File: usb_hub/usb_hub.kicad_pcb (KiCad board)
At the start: 2 copper layers, 104 x 50 mm, 143 parts, among them Q1 2N3904, U1 TPS2044B, U10 USB_A_FEMALE, U11 USB_A_FEMALE, U12 SN75240, U13 SN75240, U14 M93C46, U15 USB_A_FEMALE, U16 USB_A_FEMALE, U17 USB_A_FEMALE, U18 USB_A_FEMALE, U2 TPS2044B, U3 TUSB2077A, U4 TPS76333, U5 USB_A_MALE, U6 SN75240, U7 SN75240, U8 SN75240, U9 USB_A_FEMALE, X1 6 MHz

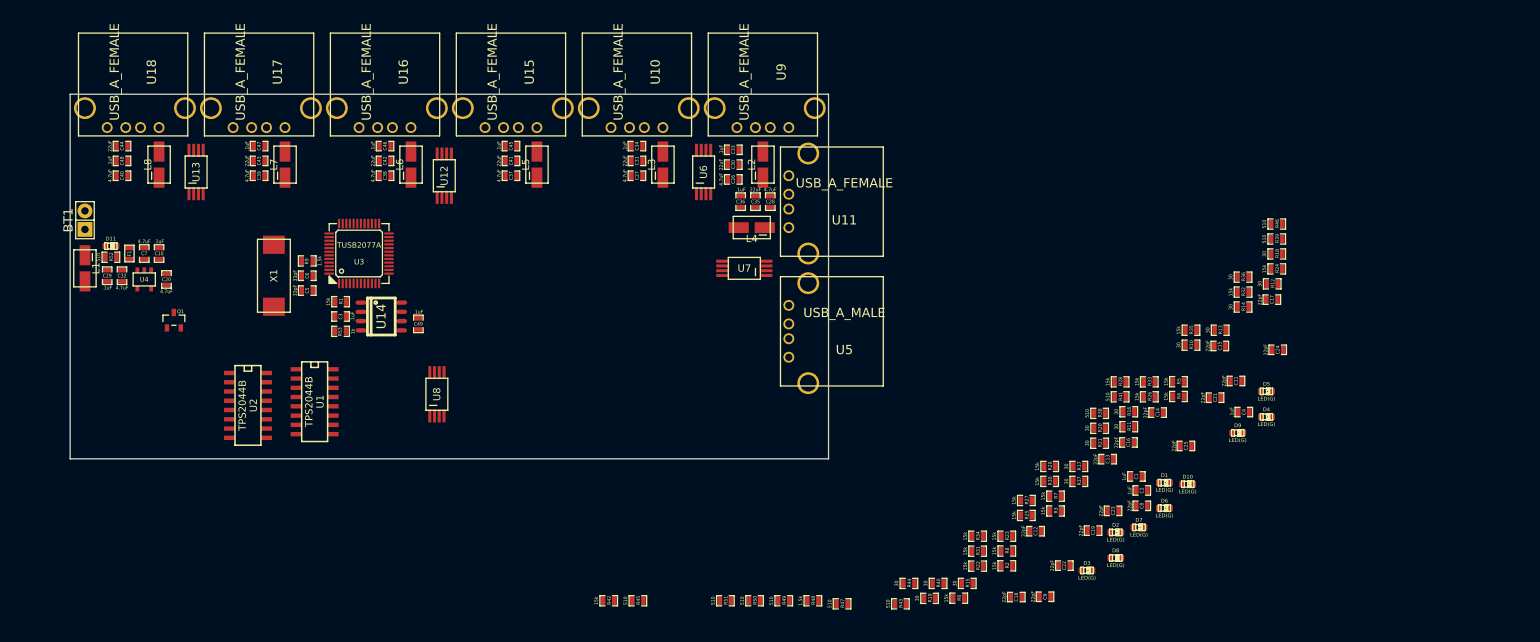
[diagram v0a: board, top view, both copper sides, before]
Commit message: need to not waste as much space on board
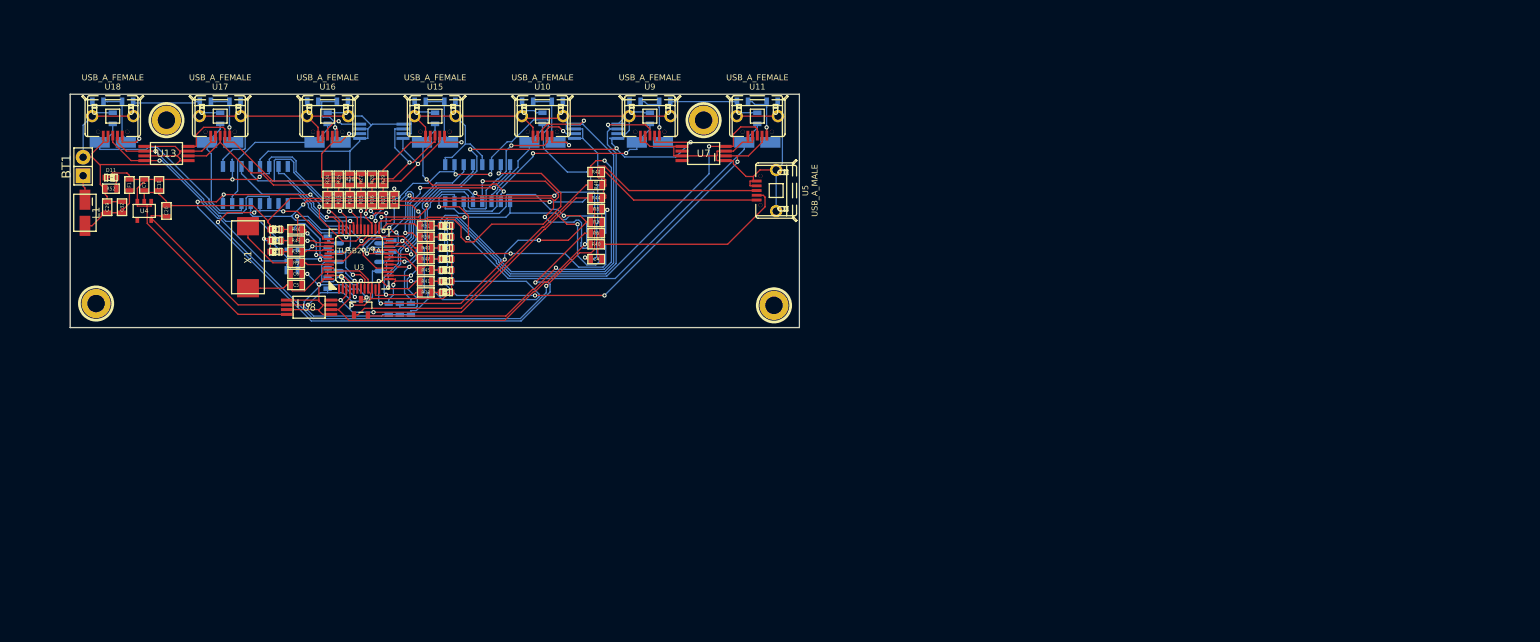
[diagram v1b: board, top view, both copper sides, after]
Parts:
- added 1PIN: P***, Connect:1pin, F.Cu at (48.8, 32.8)
- added 2PIN: P***, Connect:1pin, F.Cu at (122.4, 32.8)
- added 3PIN: P***, Connect:1pin, F.Cu at (132.1, 58.2)
- added 4PIN: P***, Connect:1pin, F.Cu at (39.1, 57.9)
- C1, C11, C12, C13, C14, C15, C16, C18, C19, C2, C21, C22, C23, C24, C25, C26, C27, C28, C3, C30, C31, C33, C34, C35, C36, C37, C38, C39, C40, C41, C42, C43, C44, C45, C46, C47, C48, C49, C8, C9: footprint SMD_Packages:SMD-0603_c -> SMD_Packages:SMD-0603; moved to B.Cu
- C10, C17, C20, C29, C32, C4, C5, C6, C7: footprint SMD_Packages:SMD-0603_c -> SMD_Packages:SMD-0603
- L2, L3, L4, L5, L6, L7, L8, U1, U12, U14, U2, U6: moved to B.Cu
- R1, R10, R11, R18, R19, R20, R21, R22, R23, R3, R30, R31, R32, R33, R34, R35, R36, R37, R4, R5, R53, R7: footprint SMD_Packages:SMD-0603_r -> SMD_Packages:SMD-0603; moved to B.Cu
- R12, R13, R14, R15, R16, R17, R2, R24, R25, R26, R27, R28, R29, R38, R39, R40, R41, R42, R43, R44, R45, R46, R47, R48, R49, R50, R51, R52, R6, R8, R9: footprint SMD_Packages:SMD-0603_r -> SMD_Packages:SMD-0603
- U10, U11, U15, U16, U17, U18, U5, U9: footprint Connect:USB_A -> ab2_usb:AB2_USB_MICRO_SMD
- moved D4 138.0 mm to (63.8, 49.3), turned to 180 degrees
- moved R39 134.5 mm to (66.5, 50.8), turned to 180 degrees
- moved R46 134.5 mm to (66.5, 47.8), turned to 180 degrees
- moved R24 130.7 mm to (70.9, 40.9), turned to 270 degrees
- moved R12 130.0 mm to (70.9, 43.7), turned to 90 degrees
- moved D6 127.7 mm to (63.8, 47.8), turned to 180 degrees
- moved C11 127.0 mm to (70.9, 43.7), turned to 90 degrees
- moved R10 124.3 mm to (65.5, 51.3), turned to 270 degrees
- moved R14 123.4 mm to (73.9, 43.7), turned to 90 degrees
- moved R13 122.2 mm to (72.4, 43.7), turned to 90 degrees
- moved D2 121.5 mm to (63.8, 50.8), turned to 180 degrees
- moved C17 121.1 mm to (80.0, 43.7), turned to 90 degrees
- moved C8 120.5 mm to (67.1, 51.3), turned to 270 degrees
- moved C15 118.0 mm to (77.0, 43.7), turned to 90 degrees
- moved R11 117.0 mm to (66.5, 49.3), turned to 180 degrees
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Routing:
- net GND: track 0.00 -> 540.9 mm, vias 0 -> 7
- net 3.3V: track 0.00 -> 127.2 mm, vias 0 -> 4
- net VCC: track 0.00 -> 125.6 mm, vias 0 -> 4
- net OC5: track 0.00 -> 100.3 mm, vias 0 -> 5
- net OC7: track 0.00 -> 86.5 mm, vias 0 -> 4
- net DP1: track 0.00 -> 67.3 mm, vias 0 -> 1
- net OUT1: track 0.00 -> 64.0 mm, vias 0 -> 2
- net OC1: track 0.00 -> 62.9 mm, vias 0 -> 5
- net DM2: track 0.00 -> 62.8 mm, vias 0 -> 3
- net OC3: track 0.00 -> 62.6 mm, vias 0 -> 4
- net DP2: track 0.00 -> 60.9 mm, vias 0 -> 1
- net OC6: track 0.00 -> 59.6 mm, vias 0 -> 3
- net DP3: track 0.00 -> 59.4 mm, vias 0 -> 1
- net DM1: track 0.00 -> 58.1 mm, vias 0 -> 3
- net DP0: track 0.00 -> 56.3 mm, vias 0 -> 3
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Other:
- board size 104 x 50 mm -> 100 x 32 mm
- net class OSH added: clearance 0.1524, trace_width 0.1524, via_dia 0.5842, via_drill 0.3302
- rule trace_min: 0.254 -> 0.1524
- rule via_min_drill: 0.508 -> 0.3302
- rule via_min_size: 0.889 -> 0.3302

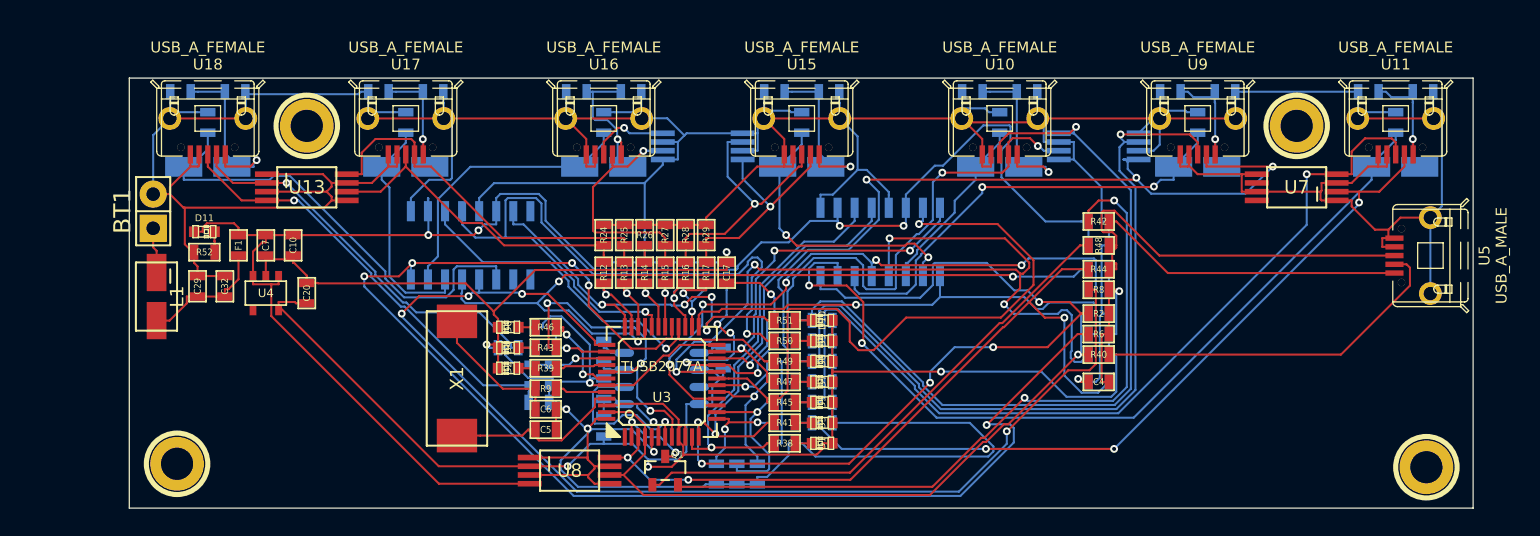
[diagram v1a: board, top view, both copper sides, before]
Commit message: made thinner approx 1x4
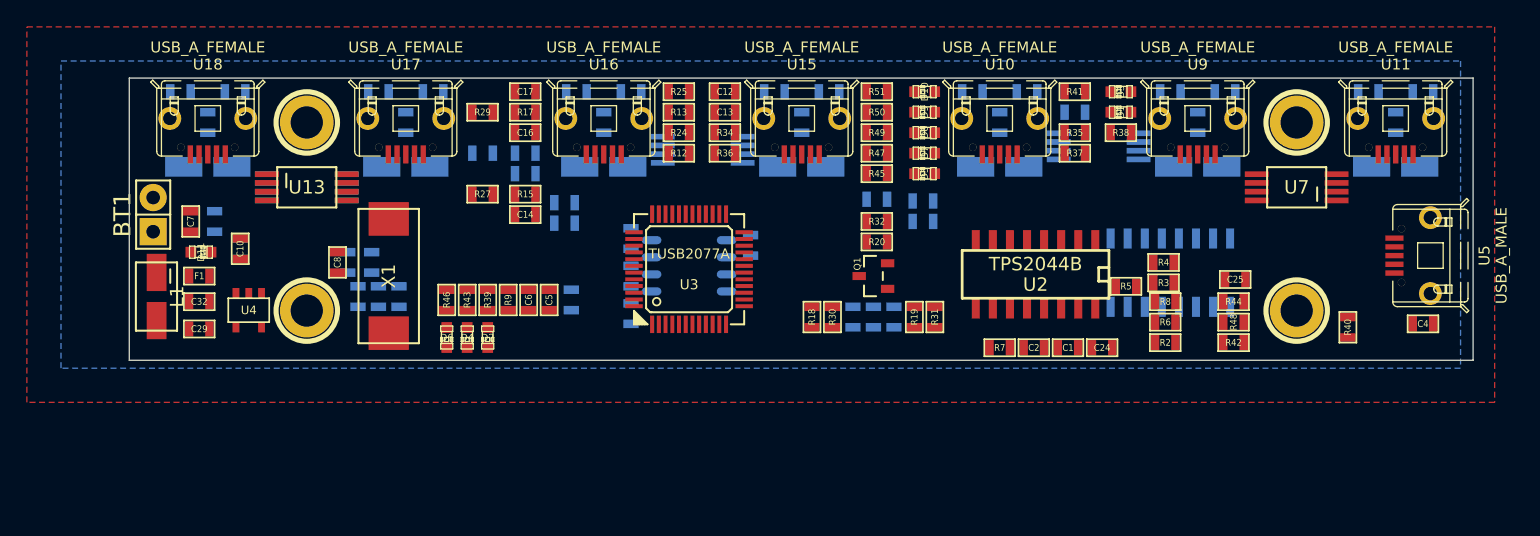
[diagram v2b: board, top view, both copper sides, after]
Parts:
- C1, C12, C13, C14, C16, C2, C24, C25, C8, R18, R19, R20, R3, R30, R31, R32, R34, R35, R36, R37, R4, R5, R7, U2: moved to F.Cu
- C20, R14, R16, R26, R28, R52, U8: moved to B.Cu
- moved U2 42.1 mm to (103.0, 43.8), turned to 180 degrees
- moved R38 34.1 mm to (109.3, 33.3), turned to 0 degrees
- moved D1 33.2 mm to (109.3, 31.8)
- moved D3 33.2 mm to (109.3, 30.2)
- moved C19 32.8 mm to (105.9, 31.8)
- moved R41 32.8 mm to (105.9, 30.2)
- moved R37 29.5 mm to (105.9, 34.8)
- moved U8 28.8 mm to (48.8, 37.3)
- moved R35 28.6 mm to (105.9, 33.3), turned to 0 degrees
- moved C4 24.5 mm to (131.8, 47.5), turned to 0 degrees
- moved U1 21.7 mm to (113.0, 43.7), turned to 180 degrees
- moved R34 21.3 mm to (79.9, 33.3)
- moved Q1 21.2 mm to (90.9, 43.9), turned to 90 degrees
- moved C17 20.1 mm to (65.0, 30.2), turned to 180 degrees
- moved R36 19.1 mm to (79.9, 34.8), turned to 180 degrees
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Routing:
- net GND: track 540.9 -> 0.00 mm, vias 7 -> 0
- net 3.3V: track 127.2 -> 0.00 mm, vias 4 -> 0
- net VCC: track 125.6 -> 0.00 mm, vias 4 -> 0
- net OC5: track 100.3 -> 0.00 mm, vias 5 -> 0
- net OC7: track 86.5 -> 0.00 mm, vias 4 -> 0
- net DP1: track 67.3 -> 0.00 mm, vias 1 -> 0
- net OUT1: track 64.0 -> 0.00 mm, vias 2 -> 0
- net OC1: track 62.9 -> 0.00 mm, vias 5 -> 0
- net DM2: track 62.8 -> 0.00 mm, vias 3 -> 0
- net OC3: track 62.6 -> 0.00 mm, vias 4 -> 0
- net DP2: track 60.9 -> 0.00 mm, vias 1 -> 0
- net OC6: track 59.6 -> 0.00 mm, vias 3 -> 0
- net DP3: track 59.4 -> 0.00 mm, vias 1 -> 0
- net DM1: track 58.1 -> 0.00 mm, vias 3 -> 0
- net DP0: track 56.3 -> 0.00 mm, vias 3 -> 0
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- added copper zone on B.Cu, net GND
- added copper zone on F.Cu, net VCC
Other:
- board size 100 x 32 mm -> 100 x 21 mm
- net class POWER added: clearance 0.1524, trace_width 1.778, via_dia 0.9652, via_drill 0.7112

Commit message: finished the usb_hub
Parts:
- added G***: LOGO, logo:logo, F.Cu at (68.5, 41.5)
- C11, C15, C18, C21, C22, C23, R16, R21, R28, R33, R52: moved to F.Cu
- C12, C4, R40, R6, R7, R8, U2: moved to B.Cu
- moved C4 88.4 mm to (43.8, 39.4), turned to 270 degrees
- moved C1 61.0 mm to (44.5, 50.2)
- moved C2 58.5 mm to (44.5, 51.7), turned to 0 degrees
- moved R6 55.0 mm to (57.8, 51.8), turned to 180 degrees
- moved R8 49.9 mm to (63.1, 51.8), turned to 180 degrees
- moved U2 40.7 mm to (62.4, 46.5), turned to 0 degrees
- moved R7 40.0 mm to (60.5, 51.8), turned to 0 degrees
- moved Q1 36.5 mm to (127.0, 49.5), turned to 180 degrees
- moved C17 35.3 mm to (96.5, 46.2), turned to 270 degrees
- moved R33 25.6 mm to (120.0, 37.1), turned to 90 degrees
- moved R21 23.9 mm to (118.5, 37.1), turned to 90 degrees
- moved R34 23.6 mm to (99.6, 46.2), turned to 90 degrees
- moved R36 21.5 mm to (98.0, 46.2), turned to 90 degrees
- moved R20 19.3 mm to (109.3, 34.8)
- moved R27 19.3 mm to (80.9, 35.1), turned to 270 degrees
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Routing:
- net 3.3V: track 0.00 -> 149.7 mm, vias 0 -> 6
- net GND: track 0.00 -> 111.7 mm, vias 0 -> 38
- net DP0: track 0.00 -> 88.3 mm, vias 0 -> 1
- net DM0: track 0.00 -> 80.8 mm, vias 0 -> 2
- net PWRON2: track 0.00 -> 59.9 mm, vias 0 -> 2
- net PWRON1: track 0.00 -> 49.3 mm, vias 0 -> 2
- net PWRON5: track 0.00 -> 48.7 mm, vias 0 -> 2
- net DP0PUR: track 0.00 -> 46.6 mm
- net PWRON7: track 0.00 -> 42.5 mm, vias 0 -> 2
- net OC5: track 0.00 -> 40.8 mm, vias 0 -> 1
- net PWRON6: track 0.00 -> 40.5 mm, vias 0 -> 2
- net DM1: track 0.00 -> 39.7 mm
- net DP1: track 0.00 -> 39.0 mm
- net Net-(C21-Pad1): track 0.00 -> 38.1 mm, vias 0 -> 2
- net Net-(C19-Pad1): track 0.00 -> 37.4 mm, vias 0 -> 3
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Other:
- board size 100 x 21 mm -> 100 x 23.5 mm
- net class Default: clearance 0.254 -> 0.1524; trace_width 0.254 -> 0.1524
- net class VCC added: clearance 0.1524, trace_width 0.8, via_dia 0.889, via_drill 0.635
- rule trace_clearance: 0.254 -> 0.1524
- board text added: "+"
- board text added: "-"

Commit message: usb_hub ready for manufacturing
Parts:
- added G***: LOGO, usb_hub:oshw, F.Cu at (38.1, 50.7)
- moved U9 0.64 mm to (115.7, 29.5)
- moved U6 0.38 mm to (107.7, 34.7)
- moved U15 0.25 mm to (85.9, 29.5)
- moved U18 0.25 mm to (41.7, 29.5)
- turned R34 to 270 degrees
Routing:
- net GND: track 111.7 -> 596.9 mm, vias 38 -> 6
- net VCC: track 8.38 -> 139.1 mm, vias 5 -> 15
- net 3.3V: track 149.7 -> 185.1 mm, vias 6 -> 5
- net DP1: track 39.0 -> 61.6 mm
- net DP5: track 12.0 -> 31.0 mm, vias 2 -> 1
- net PWRON2: track 59.9 -> 74.5 mm
- net Net-(C18-Pad1): track 14.7 -> 24.1 mm, vias 0 -> 2
- net OC2: track 29.7 -> 37.9 mm
- net OUT6: track 28.0 -> 19.8 mm
- net PWRON4: track 30.1 -> 38.0 mm, vias 1 -> 2
- net DP7: track 23.6 -> 31.3 mm, vias 1 -> 2
- net Net-(C23-Pad1): track 37.0 -> 44.6 mm, vias 3 -> 4
- net DM7: track 21.8 -> 29.0 mm, vias 1 -> 2
- net OC3: track 31.8 -> 25.6 mm
- net Net-(C19-Pad1): track 37.4 -> 31.8 mm
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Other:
- net class 4PCB added: clearance 0.1524, trace_width 0.1524, via_dia 0.635, via_drill 0.381
- net class Default: via_dia 0.889 -> 0.635; via_drill 0.635 -> 0.381
- net class OSH removed
- board text added: "SEPTA"
- board text removed: "+"
- board text removed: "-"

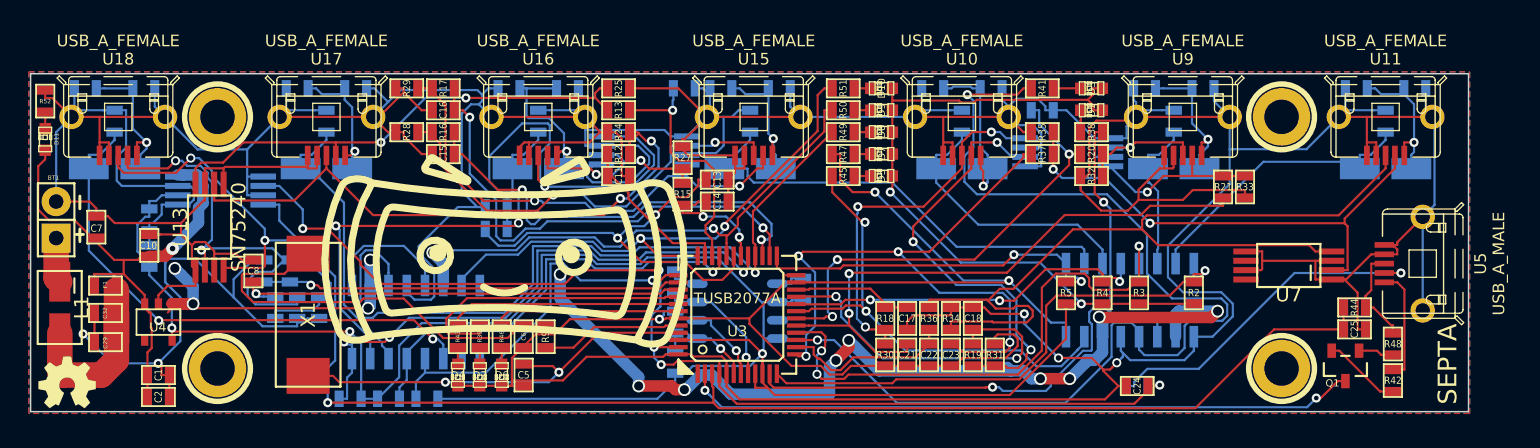
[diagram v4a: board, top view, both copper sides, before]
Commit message: usb_hub final. fixed annular ring clearance
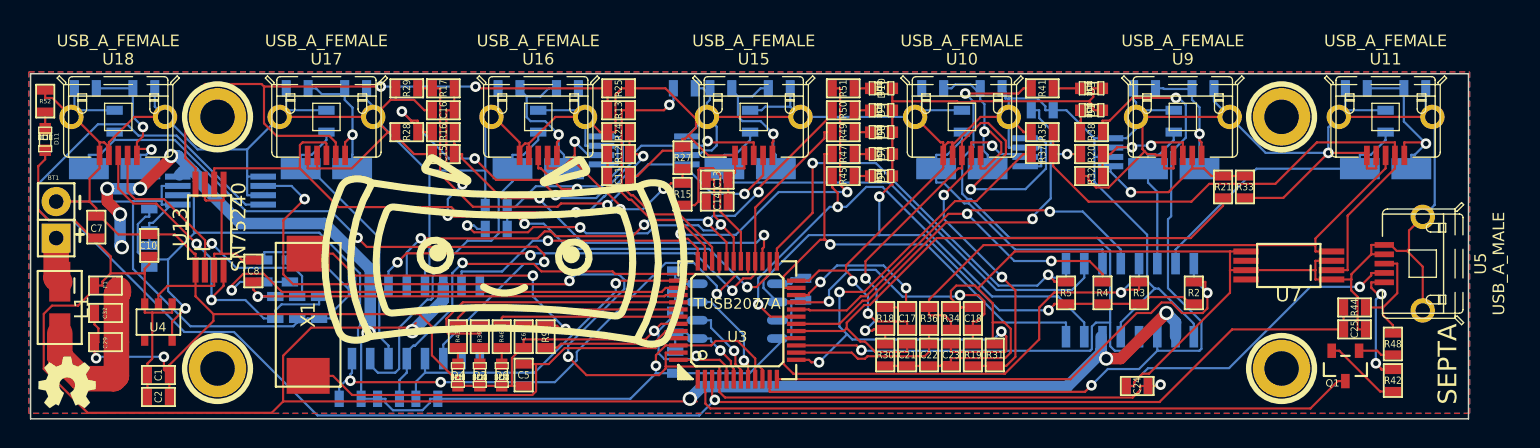
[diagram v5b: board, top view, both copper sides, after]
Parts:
- moved U3 0.38 mm to (84.7, 46.4)
- renumbered G*** to G1, G*** to G2
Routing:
- net GND: track 596.9 -> 560.7 mm, vias 6 -> 7
- net VCC: track 139.1 -> 174.7 mm, vias 15 -> 10
- net 3.3V: track 185.1 -> 153.4 mm, vias 5 -> 4
- net DP0: track 93.4 -> 123.8 mm
- net DP1: track 61.6 -> 41.6 mm
- net PWRON2: track 74.5 -> 57.4 mm
- net OC3: track 25.6 -> 39.3 mm
- net DP5: track 31.0 -> 18.4 mm
- net DM6: track 34.4 -> 46.5 mm
- net PWRON1: track 47.2 -> 59.0 mm
- net PWRON5: track 52.8 -> 41.2 mm, vias 1 -> 3
- net DP3: track 26.1 -> 36.8 mm
- net OUT7: track 37.8 -> 47.8 mm
- net DM0: track 79.1 -> 87.8 mm, vias 5 -> 4
- net DM7: track 29.0 -> 21.2 mm, vias 2 -> 1
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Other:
- board size 100 x 23.5 mm -> 100 x 24 mm
- net class 4PCB: via_dia 0.635 -> 0.7366
- net class Default: via_dia 0.635 -> 0.7366
- net class POWER: via_dia 0.9652 -> 1.0668
- net class VCC: trace_width 0.8 -> 0.8001; via_dia 0.889 -> 0.9906
- rule pad_to_mask_clearance: 0 -> 0.0508

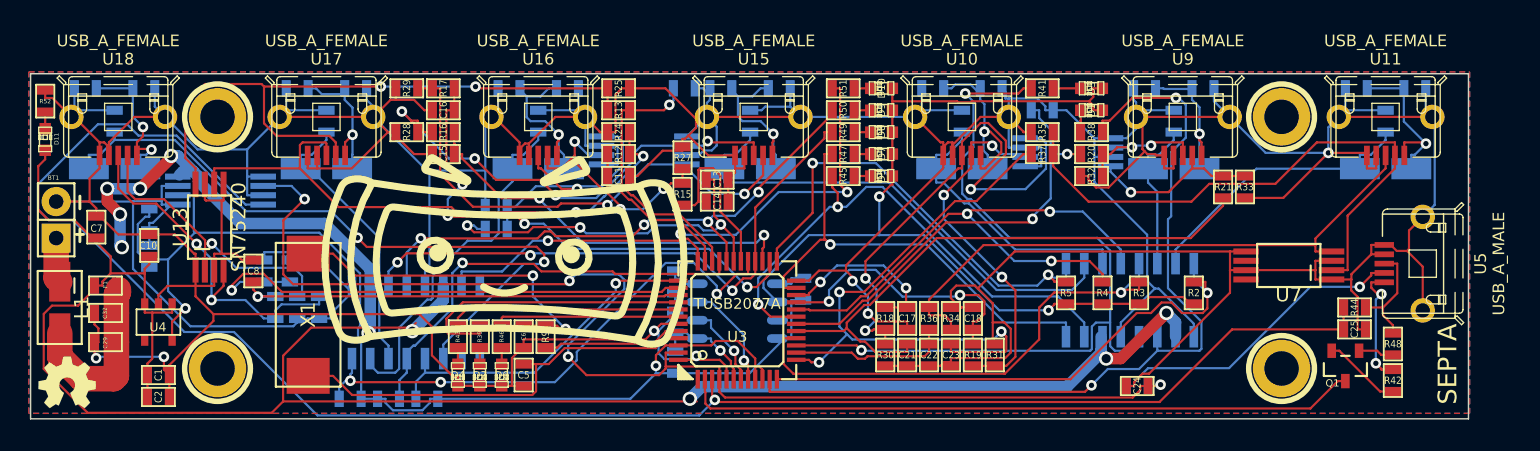
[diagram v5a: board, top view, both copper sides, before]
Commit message: moved the trace away from the edge
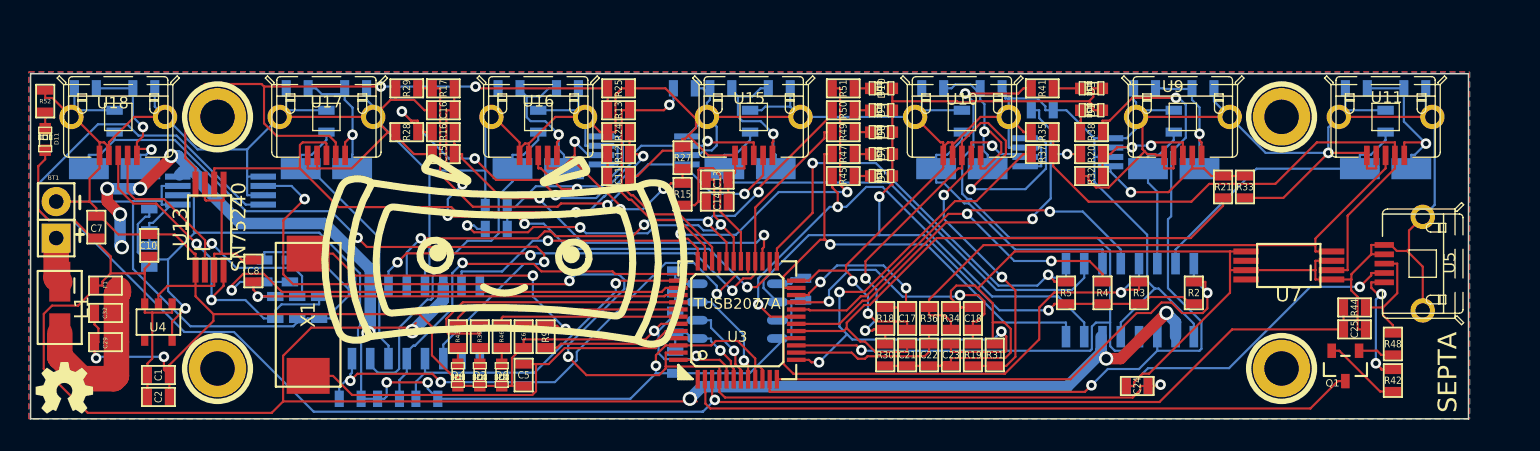
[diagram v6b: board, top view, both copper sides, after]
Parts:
- moved G1 0.43 mm to (37.9, 51.1)
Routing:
- net 3.3V: track 153.4 -> 154.2 mm, vias 4 -> 6
